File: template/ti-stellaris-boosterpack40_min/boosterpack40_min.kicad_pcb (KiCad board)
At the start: 2 copper layers, 50.8 x 34.3 mm, 4 parts, among them J1 TI_BOOSTER_40_J1, J2 TI_BOOSTER_40_J2, J3 TI_BOOSTER_40_J3, J4 TI_BOOSTER_40_J4

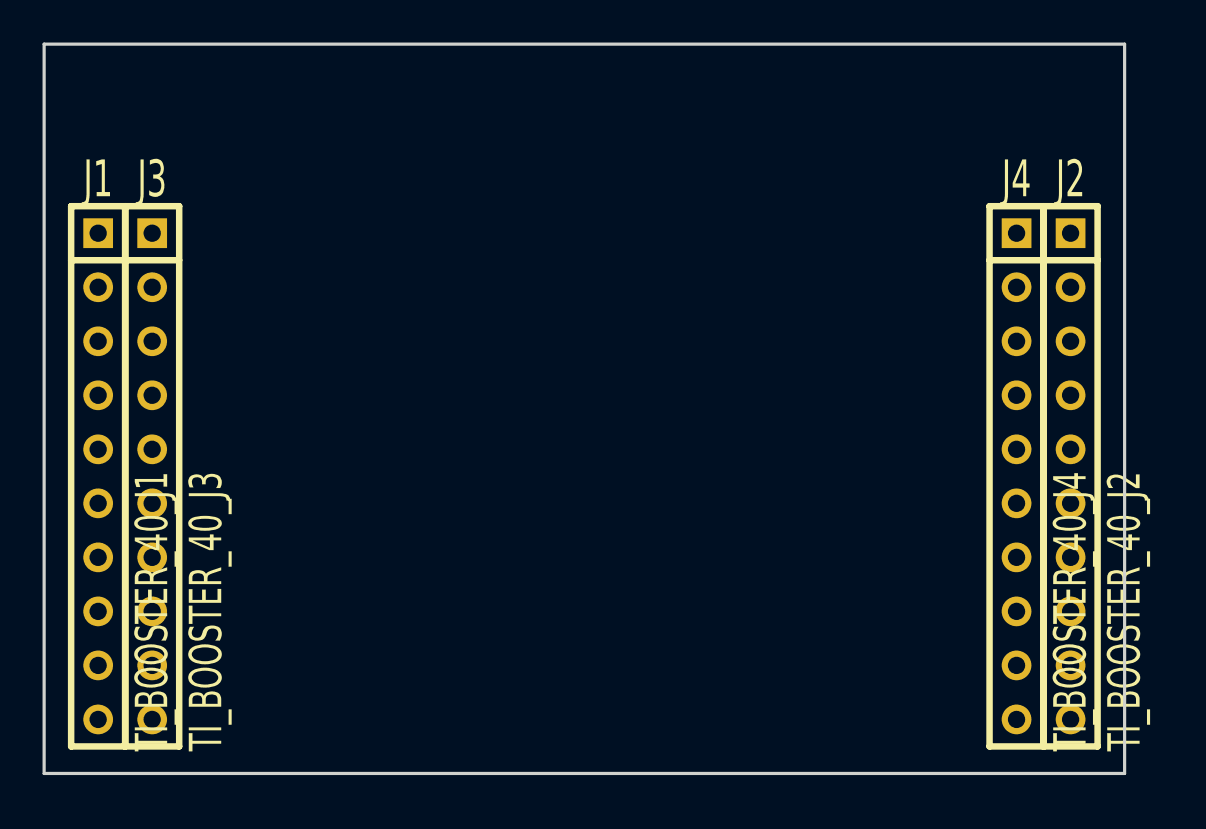
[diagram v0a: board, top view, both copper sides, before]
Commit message: fix template
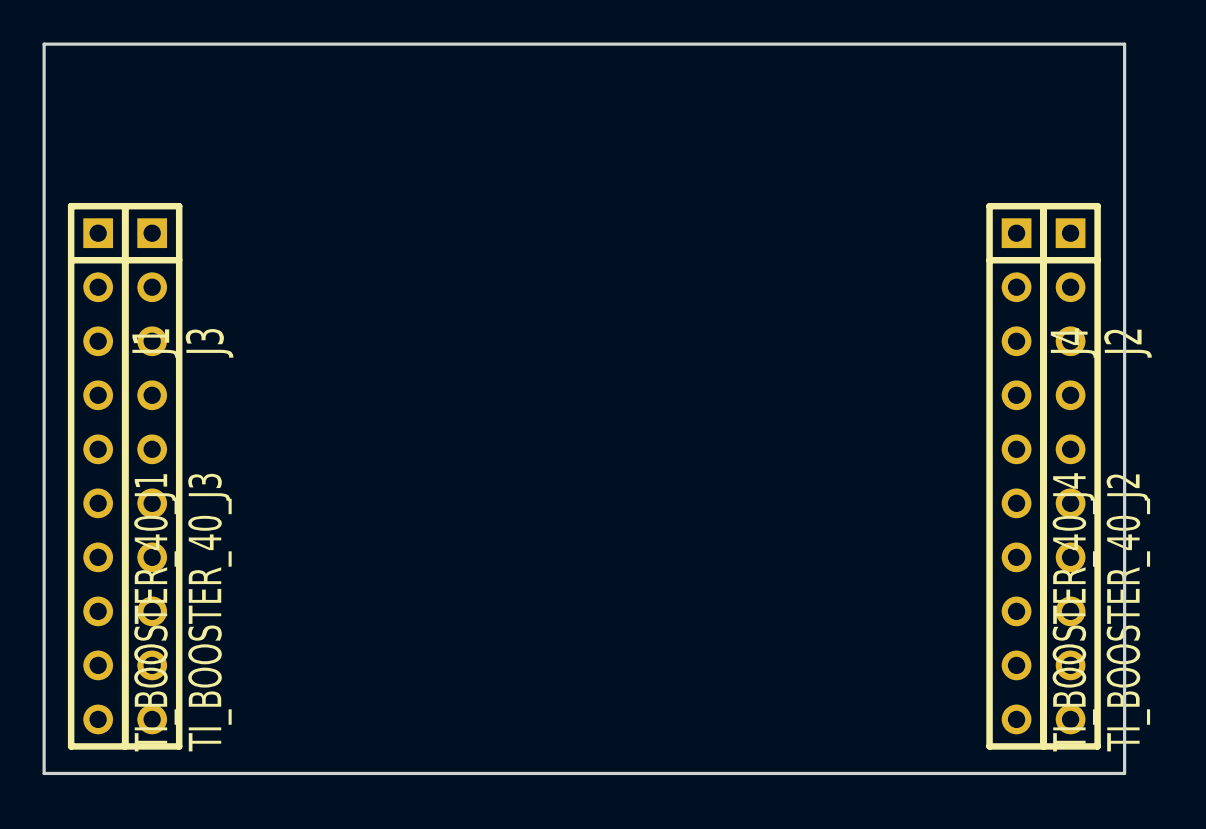
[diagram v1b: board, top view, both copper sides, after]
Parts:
- J1, J2, J3, J4: footprint SIL-10 -> Connect:SIL-10
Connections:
- J1 pad 1: VCC -> (no net)
- J3 pad 1: +5V -> (no net)
